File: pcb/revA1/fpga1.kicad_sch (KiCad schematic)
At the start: 21 parts, among them U1 XC6SLX25-FTG256

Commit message: revA1, WIP
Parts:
- removed TP2, TP3, TP6, TP7: TestPoint, TestPoint:TestPoint_Pad_D1.5mm, symbol Connector:TestPoint
- T2: renamed from TP1; value TestPoint -> TestPoint2
- renumbered TP4 to T3, TP5 to T4
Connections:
- net MA10: now also U1.P16 (IO_L48N_M1DQ9_1); no longer U1.R16 (IO_L49N_M1DQ11_1)
- net MA12: now also U1.R16 (IO_L49N_M1DQ11_1); no longer U1.P16 (IO_L48N_M1DQ9_1)
- net MA13: now also U1.R14 (IO_L50P_M1UDQS_1); no longer U1.P15 (IO_L48P_HDC_M1DQ8_1)
- net MA14: now also U1.T14 (IO_L51P_M1DQ12_1); no longer U1.N16 (IO_L45N_A0_M1LDQSN_1)
- net MA15: now also U1.T15 (IO_L50N_M1UDQSN_1); no longer U1.N14 (IO_L45P_A1_M1LDQS_1)
- net MA19: now also U1.N14 (IO_L45P_A1_M1LDQS_1); no longer U1.T14 (IO_L51P_M1DQ12_1)
- net MA8: now also U1.N16 (IO_L45N_A0_M1LDQSN_1); no longer U1.T15 (IO_L50N_M1UDQSN_1)
- net MA9: now also U1.P15 (IO_L48P_HDC_M1DQ8_1); no longer U1.R14 (IO_L50P_M1UDQS_1)
- net ~{SD_DET}: now reaches U1.A11 (IO_L39N_0)
- net SD_CLK: now reaches U1.B12 (IO_L62P_0)
- net SD_DO: now reaches U1.B14 (IO_L65P_SCP3_0)
- net SD_DI: now reaches U1.F13 (IO_L32P_A17_M1A8_1)
- net ~{SD_CS}: now reaches U1.F14 (IO_L32N_A16_M1A9_1)
- net CFG5: now reaches U1.H14 (IO_L39N_M1ODT_1)
- net ~{BTN_NMI}: now reaches U1.L13 (IO_L53N_VREF_1)
- net ~{PSRAM_CS}: now reaches U1.M13 (IO_L74P_AWAKE_1)
- no-connect marks 40 -> 36

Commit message: revA1
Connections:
- net ~{oRST}: now reaches U1.C5 (IO_L3N_0)
- no-connect marks 36 -> 35
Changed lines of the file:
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@@
-	)
-	(no_connect
-		(at 36.83 57.15)
 	)
 	(no_connect
@@
 		(pts
 			(xy 266.7 68.58) (xy 266.7 71.12)
+		)
+		(stroke
+			(width 0)
+			(type default)
+		)
+	)
+	(wire
+		(pts
+			(xy 33.02 57.15) (xy 36.83 57.15)
 		)
 		(stroke
@@
 			)
 		)
+	)
+	(global_label "~{oRST}"
+		(shape input)
+		(at 33.02 57.15 180)
+		(fields_autoplaced yes)
+		(effects
+			(font
+				(size 0.9906 0.9906)
+			)
+			(justify right)
+		)
+		(property "Intersheetrefs" "${INTERSHEET_REFS}"
+			(at 27.0325 57.15 0)
+			(hide yes)
+			(show_name no)
+			(do_not_autoplace no)
+			(effects
+				(font
+					(size 0.9906 0.9906)
+				)
+				(justify right)
+			)
+		)

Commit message: Small improvements to the revA1
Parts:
- T2, T3: now left out of the parts list
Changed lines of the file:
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@@
 	(title_block
 		(title "Karabas-MegaBuzz")
-		(date "2026-05-27")
+		(date "2026-05-29")
 		(rev "A1")
 		(company "Andy Karpov")
@@
 		(body_style 1)
 		(exclude_from_sim no)
-		(in_bom yes)
+		(in_bom no)
 		(on_board yes)
 		(in_pos_files yes)
@@
 		(body_style 1)
 		(exclude_from_sim no)
-		(in_bom yes)
+		(in_bom no)
 		(on_board yes)
 		(in_pos_files yes)

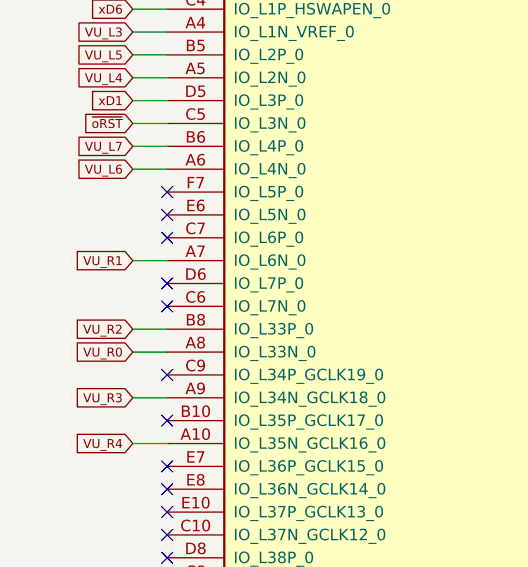
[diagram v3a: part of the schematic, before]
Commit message: Fixed missing LED1 connection, new revA1 release
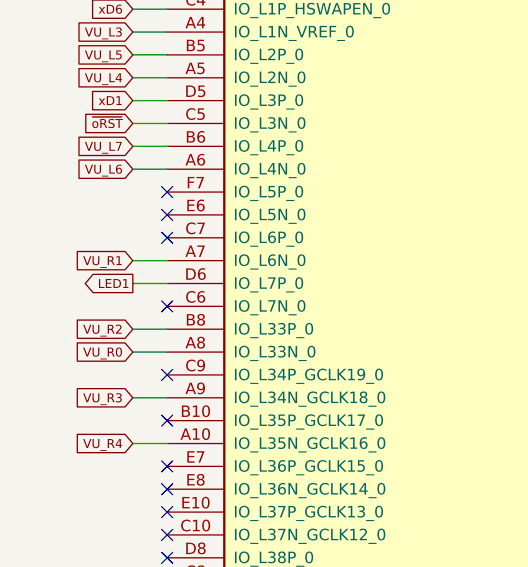
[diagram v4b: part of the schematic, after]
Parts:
- T4: now left out of the parts list
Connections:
- net LED1: now reaches U1.D6 (IO_L7P_0)
- no-connect marks 35 -> 34
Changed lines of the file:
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@@
 	)
 	(no_connect
-		(at 36.83 74.93)
-	)
-	(no_connect
 		(at 138.43 118.11)
 	)
@@
 	(wire
 		(pts
+			(xy 33.02 74.93) (xy 36.83 74.93)
+		)
+		(stroke
+			(width 0)
+			(type default)
+		)
+	)
+	(wire
+		(pts
 			(xy 210.82 66.04) (xy 210.82 68.58)
 		)
@@
 		)
 	)
+	(global_label "LED1"
+		(shape output)
+		(at 33.02 74.93 180)
+		(fields_autoplaced yes)
+		(effects
+			(font
+				(size 0.9906 0.9906)
+			)
+			(justify right)
+		)
+		(property "Intersheetrefs" "${INTERSHEET_REFS}"
+			(at 26.9853 74.93 0)
+			(hide yes)
+			(show_name no)
+			(do_not_autoplace no)
+			(effects
+				(font
+					(size 0.9906 0.9906)
+				)
+				(justify right)
+			)
+		)
+	)
 	(global_label "VU_L4"
 		(shape input)
@@
 		(body_style 1)
 		(exclude_from_sim no)
-		(in_bom yes)
+		(in_bom no)
 		(on_board yes)
 		(in_pos_files yes)
